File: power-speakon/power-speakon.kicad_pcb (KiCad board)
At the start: 4 copper layers, 65 x 24 mm, 18 parts, among them J101 NL4MDXX-V-3, J102 NL4MDXX-V-3, J103 WAGO 2601-1101, J104 WAGO 2601-1101, Q201 BSC010N04LS, Q202 BSC010N04LS, U201 LM74502-Q1

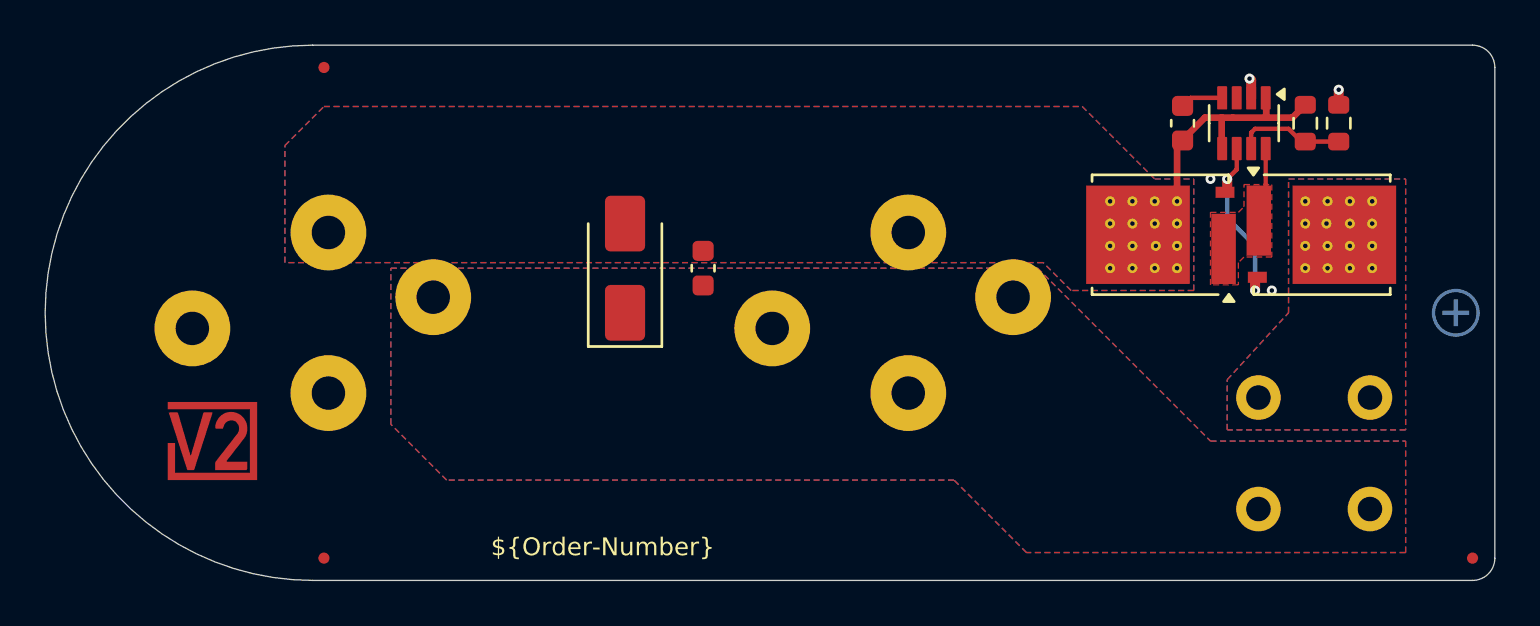
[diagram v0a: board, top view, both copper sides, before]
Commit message: Update power symbols
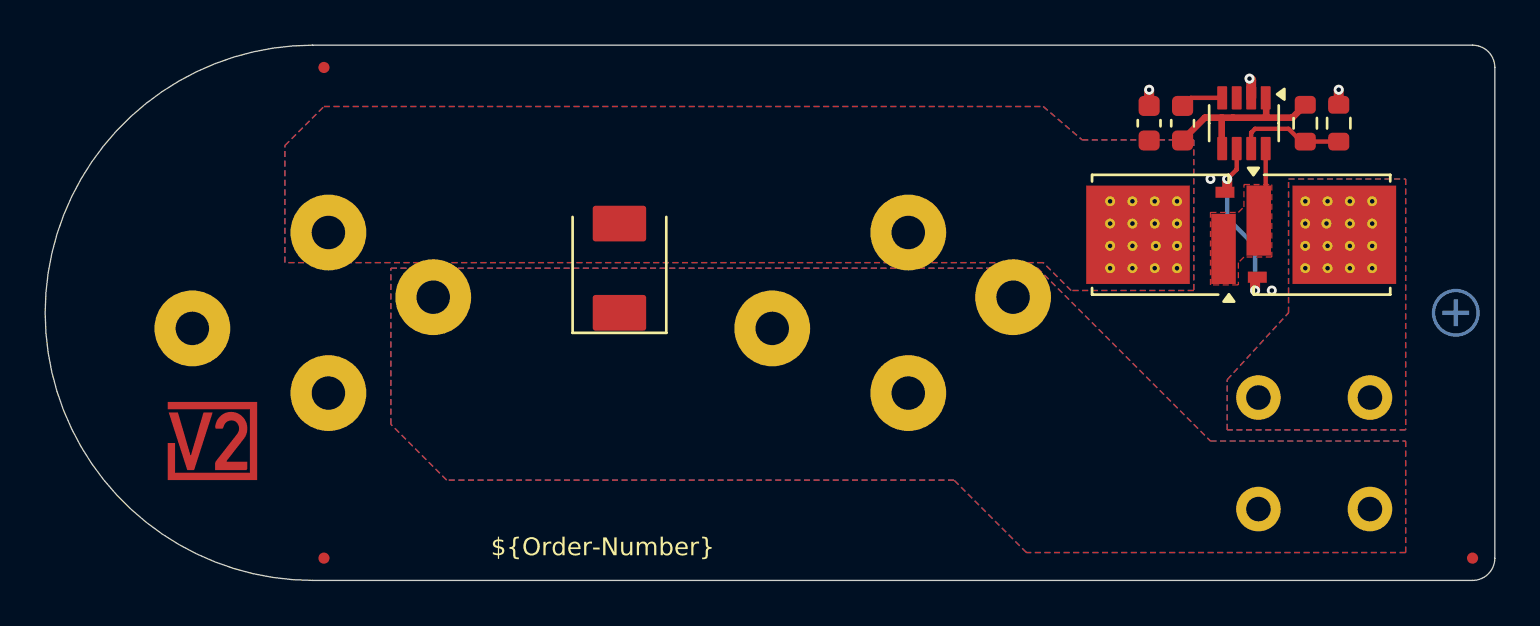
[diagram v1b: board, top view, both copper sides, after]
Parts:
- C201, C202: footprint Capacitor_SMD:C_0603_1608Metric -> V2_Capacitor_SMD:C_0603
- FID101, FID102, FID103: value Fiducial -> Fiducial_Paste
- INFO101: value ORDER-NUMBER -> Order_Number
- R201, R202: footprint Resistor_SMD:R_0603_1608Metric -> V2_Resistor_SMD:R_0603
- TVS101: value SMAJ36CA -> SMBJ36CA; footprint Diode_SMD:D_SMA -> V2_Diode_SMD:D_SMB
- moved C201 21.0 mm to (152.2, 83.2), turned to 90 degrees
- moved TVS101 0.25 mm to (128.5, 89.8)
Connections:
- net /+24V-Socket renamed /+24V-Supply
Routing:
- net /+24V-Supply: track 11.3 -> 8.83 mm
- net GND: track 1.57 -> 2.29 mm, vias 4 -> 5

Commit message: Fix WAGOs
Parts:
- moved J104 1.50 mm to (160.2, 98.8)
- moved ICON102 0.25 mm to (166.0, 91.5)
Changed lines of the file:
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@@
 	(footprint "V2_Artwork:Plus_Small"
 		(layer "B.Cu")
-		(at 166 91.75 180)
+		(at 166 91.5 180)
 		(property "Reference" "ICON102"
 			(at 0 2.5 0)
@@
 	(footprint "V2_Connector_WAGO:2601-1101"
 		(layer "B.Cu")
-		(at 160.25 100.25 -90)
+		(at 160.25 98.75 -90)
 		(property "Reference" "J104"
 			(at 0.1 12 90)
@@
 		)
 		(fp_text user "${REFERENCE}"
-			(at 0 0 180)
-			(layer "B.Fab")
-			(effects
+			(at 0 0 0)
+			(layer "B.Fab")
+			(effects

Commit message: Refresh
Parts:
- J101, J102: footprint V2_Connector_Audio:Jack_speakON_Neutrik_NL4MDXX-V-3_Vertical -> V2_Connector_SpeakOn:Jack_speakON_Neutrik_NL4MDXX-V-3_Vertical
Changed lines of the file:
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@@
 				(font
 					(size 0.5 0.5)
-					(thickness 0.05)
+					(thickness 0.1)
+					(bold yes)
 				)
 			)
@@
 		)
 		(fp_rect
-			(start -1.48 -0.73)
-			(end 1.48 0.73)
+			(start -1.23 -0.73)
+			(end 1.23 0.73)
 			(stroke
 				(width 0.05)
@@
 		)
 		(pad "1" smd roundrect
-			(at -0.775 0 90)
-			(size 0.9 0.95)
+			(at -0.7 0 90)
+			(size 0.7 0.8)
 			(layers "F.Cu" "F.Mask" "F.Paste")
-			(roundrect_rratio 0.25)
+			(roundrect_rratio 0.1428571429)
 			(net 12 "/+24V-Supply")
 			(pintype "passive")
 		)
 		(pad "2" smd roundrect
-			(at 0.775 0 90)
-			(size 0.9 0.95)
+			(at 0.7 0 90)
+			(size 0.7 0.8)
 			(layers "F.Cu" "F.Mask" "F.Paste")
-			(roundrect_rratio 0.25)
+			(roundrect_rratio 0.1428571429)
 			(net 1 "GND")
 			(pintype "passive")
@@
 		)
 		(fp_rect
-			(start -1.48 -0.73)
-			(end 1.48 0.73)
+			(start -1.23 -0.73)
+			(end 1.23 0.73)
 			(stroke
 				(width 0.05)
@@
 		)
 		(pad "1" smd roundrect
-			(at -0.825 0 90)
-			(size 0.8 0.95)
+			(at -0.75 0 90)
+			(size 0.75 0.95)
 			(layers "F.Cu" "F.Mask" "F.Paste")
-			(roundrect_rratio 0.25)
+			(roundrect_rratio 0.1333333333)
 			(net 10 "/Polarity Protection/Overvoltage")
 			(pintype "passive")
 		)
 		(pad "2" smd roundrect
-			(at 0.825 0 90)
-			(size 0.8 0.95)
+			(at 0.75 0 90)
+			(size 0.75 0.95)
 			(layers "F.Cu" "F.Mask" "F.Paste")
-			(roundrect_rratio 0.25)
+			(roundrect_rratio 0.1333333333)
 			(net 1 "GND")
 			(pintype "passive")
@@
 			(effects
 				(font
-					(size 0.75 0.75)
+					(size 0.5 0.5)
 					(thickness 0.1)
 				)
@@
 				(font
 					(size 0.5 0.5)
-					(thickness 0.05)
+					(thickness 0.1)
+					(bold yes)
 				)
 			)
@@
 			(effects
 				(font
-					(size 0.75 0.75)
+					(size 0.5 0.5)
 					(thickness 0.1)
 				)
@@
 		)
 		(fp_rect
-			(start -1.48 -0.73)
-			(end 1.48 0.73)
+			(start -1.23 -0.73)
+			(end 1.23 0.73)
 			(stroke
 				(width 0.05)
@@
 		)
 		(pad "1" smd roundrect
-			(at -0.775 0 90)
-			(size 0.9 0.95)
+			(at -0.7 0 90)
+			(size 0.7 0.8)
 			(layers "F.Cu" "F.Mask" "F.Paste")
-			(roundrect_rratio 0.25)
+			(roundrect_rratio 0.1428571429)
 			(net 12 "/+24V-Supply")
 			(pintype "passive")
 		)
 		(pad "2" smd roundrect
-			(at 0.775 0 90)
-			(size 0.9 0.95)
+			(at 0.7 0 90)
+			(size 0.7 0.8)
 			(layers "F.Cu" "F.Mask" "F.Paste")
-			(roundrect_rratio 0.25)
+			(roundrect_rratio 0.1428571429)
 			(net 7 "Net-(U201-VCAP)")
 			(pintype "passive")
@@
 		)
 		(fp_rect
-			(start -1.48 -0.73)
-			(end 1.48 0.73)
+			(start -1.23 -0.73)
+			(end 1.23 0.73)
 			(stroke
 				(width 0.05)
@@
 		)
 		(pad "1" smd roundrect
-			(at -0.825 0 270)
-			(size 0.8 0.95)
+			(at -0.75 0 270)
+			(size 0.75 0.95)
 			(layers "F.Cu" "F.Mask" "F.Paste")
-			(roundrect_rratio 0.25)
+			(roundrect_rratio 0.1333333333)
 			(net 12 "/+24V-Supply")
 			(pintype "passive")
 		)
 		(pad "2" smd roundrect
-			(at 0.825 0 270)
-			(size 0.8 0.95)
+			(at 0.75 0 270)
+			(size 0.75 0.95)
 			(layers "F.Cu" "F.Mask" "F.Paste")
-			(roundrect_rratio 0.25)
+			(roundrect_rratio 0.1333333333)
 			(net 10 "/Polarity Protection/Overvoltage")
 			(pintype "passive")
@@
 			(effects
 				(font
-					(size 0.75 0.75)
+					(size 0.5 0.5)
 					(thickness 0.1)
 					(bold yes)
@@
 		)
 		(embedded_fonts no)
-		(model "/Users/kay/Documents/KiCad/9.0/versioduo.kicad/3dmodels/V2_Connector_WAGO.3dshapes/2601-1101.stp"
+		(model "../../3dmodels/V2_Connector_WAGO.3dshapes/2601-1101.stp"
 			(offset
 				(xyz 1.36 -1.9 0)
@@
 		(embedded_fonts no)
 	)
-	(footprint "V2_Connector_Audio:Jack_speakON_Neutrik_NL4MDXX-V-3_Vertical"
+	(footprint "V2_Connector_SpeakOn:Jack_speakON_Neutrik_NL4MDXX-V-3_Vertical"
 		(layer "B.Cu")
 		(at 140.75 91.75 180)
@@
 			(layer "B.Fab")
 		)
+		(fp_text user "${REFERENCE}"
+			(at 0 0 0)
+			(layer "B.Fab")
+			(effects
+				(font
+					(size 0.75 0.75)
+					(thickness 0.1)
+				)
+				(justify mirror)
+			)
+		)
 		(pad "1+" thru_hole circle
 			(at -0.7 3.6 180)
@@
 		)
 	)
-	(footprint "V2_Connector_Audio:Jack_speakON_Neutrik_NL4MDXX-V-3_Vertical"
+	(footprint "V2_Connector_SpeakOn:Jack_speakON_Neutrik_NL4MDXX-V-3_Vertical"
 		(layer "B.Cu")
 		(at 114.75 91.75 180)
@@
 			(layer "B.Fab")
 		)
+		(fp_text user "${REFERENCE}"
+			(at 0 0 0)
+			(layer "B.Fab")
+			(effects
+				(font
+					(size 0.75 0.75)
+					(thickness 0.1)
+				)
+				(justify mirror)
+			)
+		)
 		(pad "1+" thru_hole circle
 			(at -0.7 3.6 180)
@@
 		)
 		(fp_text user "${REFERENCE}"
-			(at 0 0 0)
+			(at 0 0 180)
 			(layer "B.Fab")
 			(effects
 				(font
-					(size 0.75 0.75)
+					(size 0.5 0.5)
 					(thickness 0.1)
 					(bold yes)
@@
 		)
 		(embedded_fonts no)
-		(model "/Users/kay/Documents/KiCad/9.0/versioduo.kicad/3dmodels/V2_Connector_WAGO.3dshapes/2601-1101.stp"
+		(model "../../3dmodels/V2_Connector_WAGO.3dshapes/2601-1101.stp"
 			(offset
 				(xyz 1.36 -1.9 0)
@@
 		)
 	)
-	(gr_arc
-		(start 114.75 103.75)
-		(mid 102.75 91.75)
-		(end 114.75 79.75)
-		(stroke
-			(width 0.05)
-			(type solid)
-		)
-		(layer "Edge.Cuts")
-	)
 	(gr_line
 		(start 114.75 79.75)
@@
 		(layer "Edge.Cuts")
 	)
-	(gr_line
-		(start 167.75 80.75)
-		(end 167.75 102.75)
+	(gr_arc
+		(start 114.75 103.75)
+		(mid 102.75 91.75)
+		(end 114.75 79.75)
 		(stroke
 			(width 0.05)
@@
 		(layer "Edge.Cuts")
 	)
-	(gr_arc
-		(start 167.75 102.75)
-		(mid 167.457107 103.457107)
+	(gr_line
+		(start 114.75 103.75)
 		(end 166.75 103.75)
 		(stroke
@@
 	)
 	(gr_line
-		(start 114.75 103.75)
+		(start 167.75 80.75)
+		(end 167.75 102.75)
+		(stroke
+			(width 0.05)
+			(type solid)
+		)
+		(layer "Edge.Cuts")
+	)
+	(gr_arc
+		(start 167.75 102.75)
+		(mid 167.457107 103.457107)
 		(end 166.75 103.75)
 		(stroke

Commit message: Update library
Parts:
- J101, J102: footprint V2_Connector_SpeakOn:Jack_speakON_Neutrik_NL4MDXX-V-3_Vertical -> V2_Connector_SpeakOn:NL4MDXX-V-3
- TVS101: value SMBJ36CA -> SMBJ33CA
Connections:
- net +24V renamed +28V
- net /+24V-Supply renamed /+28V-Supply

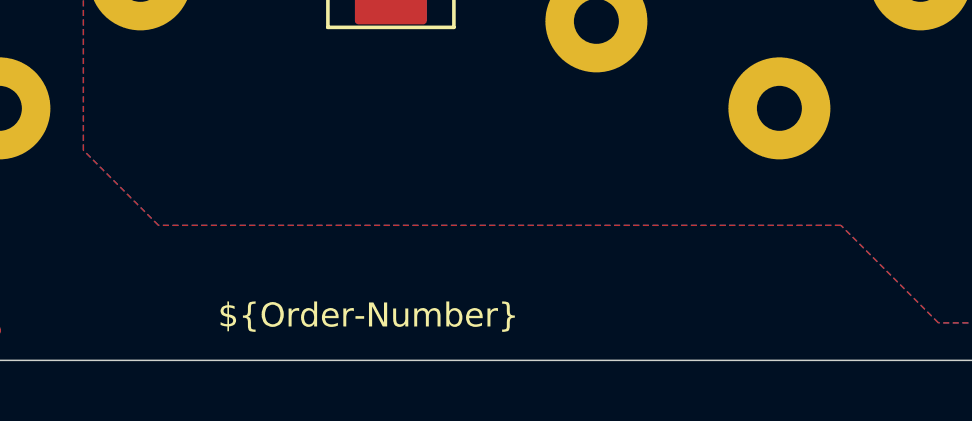
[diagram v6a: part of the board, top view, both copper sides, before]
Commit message: Replace Order_Number
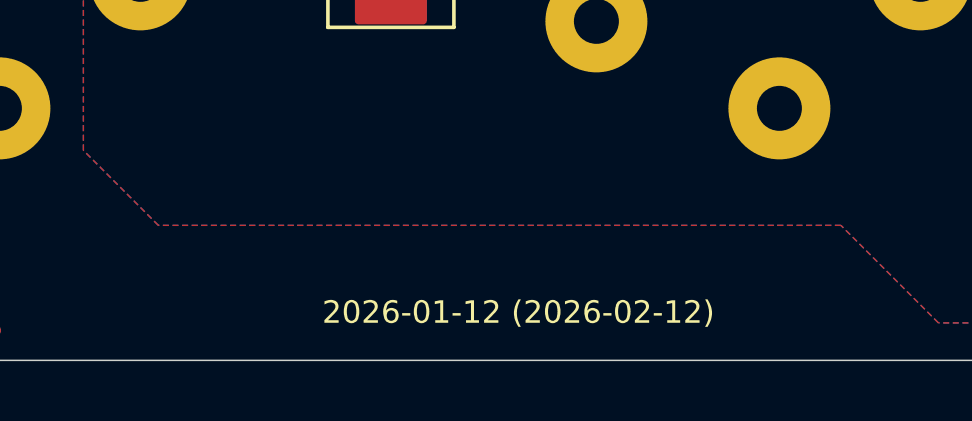
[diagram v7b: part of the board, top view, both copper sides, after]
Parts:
- INFO101: value Order_Number -> ~; footprint V2_Production:Order_Number -> V2_Production:Revision
- moved INFO101 5.00 mm to (132.8, 102.2)
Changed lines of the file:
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@@
 	(paper "A4")
 	(title_block
-		(date "2026-02-10")
+		(date "2026-02-12")
 		(rev "2026-01-12")
 	)
@@
 		)
 	)
-	(property "Order-Number" "JLCJLCJLCJLC")
 	(net 0 "")
 	(net 1 "GND")
@@
 			)
 		)
-		(property "Description" ""
+		(property "Description" "Transient Voltage Suppressor Diode, Bidirectional, 36.7-40.6V"
 			(at 0 0 90)
 			(unlocked yes)
@@
 			)
 		)
-		(property "Description" ""
+		(property "Description" "Unpolarized capacitor, small symbol"
 			(at 0 0 90)
 			(layer "F.Fab")
@@
 			)
 		)
-		(property "Description" ""
+		(property "Description" "Fiducial Marker"
 			(at 0 0 0)
 			(unlocked yes)
@@
 			)
 		)
-		(property "Description" ""
+		(property "Description" "Resistor, small symbol"
 			(at 0 0 90)
 			(layer "F.Fab")
@@
 		)
 	)
-	(footprint "V2_Production:Order_Number"
+	(footprint "V2_Production:Revision"
 		(layer "F.Cu")
-		(at 127.75 102.25)
+		(at 132.75 102.15)
 		(property "Reference" "INFO101"
 			(at 0 -1.77 0)
@@
 			)
 		)
-		(property "Value" "Order_Number"
+		(property "Value" "~"
 			(at 0 2.27 0)
 			(unlocked yes)
@@
 		(sheetname "/")
 		(sheetfile "power-speakon.kicad_sch")
-		(attr exclude_from_pos_files exclude_from_bom)
-		(fp_rect
-			(start -7 -0.75)
-			(end 7 0.75)
-			(stroke
-				(width 0.05)
-				(type default)
+		(attr exclude_from_pos_files exclude_from_bom allow_missing_courtyard)
+		(fp_text user "${REVISION} (${ISSUE_DATE})"
+			(at 0 0 0)
+			(unlocked yes)
+			(layer "F.SilkS")
+			(effects
+				(font
+					(size 0.75 0.75)
+					(thickness 0.1)
+				)
 			)
-			(fill no)
-			(layer "F.CrtYd")
 		)
-		(fp_text user "${Order-Number}"
+		(fp_text user "${REVISION} (${ISSUE_DATE})"
 			(at 0 0 0)
 			(unlocked yes)
-			(layer "F.SilkS")
+			(layer "F.Fab")
 			(effects
 				(font
-					(size 0.8 0.8)
-					(thickness 0.12)
+					(size 0.75 0.75)
+					(thickness 0.1)
 				)
 			)
@@
 			)
 		)
-		(property "Description" ""
+		(property "Description" "Fiducial Marker"
 			(at 0 0 0)
 			(unlocked yes)
@@
 			)
 		)
-		(property "Description" ""
+		(property "Description" "Reverse Polarity Protection Controller"
 			(at 0 0 270)
 			(unlocked yes)
@@
 			)
 		)
-		(property "Description" ""
+		(property "Description" "Unpolarized capacitor, small symbol"
 			(at 0 0 90)
 			(layer "F.Fab")
@@
 			)
 		)
-		(property "Description" ""
+		(property "Description" "Resistor, small symbol"
 			(at 0 0 270)
 			(layer "F.Fab")
@@
 			)
 		)
-		(property "Description" ""
+		(property "Description" "Fiducial Marker"
 			(at 0 0 0)
 			(unlocked yes)
@@
 			)
 		)
-		(property "Sim.Enable" "0"
-			(at 0 0 0)
-			(unlocked yes)
-			(layer "F.Fab")
-			(hide yes)
-			(effects
-				(font
-					(size 1 1)
-					(thickness 0.15)
-				)
-			)
-		)
 		(sheetname "/")
 		(sheetfile "power-speakon.kicad_sch")
@@
 			)
 		)
-		(property "Sim.Enable" "0"
-			(at 0 0 180)
-			(unlocked yes)
-			(layer "B.Fab")
-			(hide yes)
-			(effects
-				(font
-					(size 1 1)
-					(thickness 0.15)
-				)
-				(justify mirror)
-			)
-		)
 		(sheetname "/")
 		(sheetfile "power-speakon.kicad_sch")
@@
 			)
 		)
-		(property "Datasheet" ""
+		(property "Datasheet" "https://www.neutrik.com/en/product/nl4mdxx-v-3"
 			(at -0.7 3.6 0)
 			(unlocked yes)
@@
 			)
 		)
-		(property "Description" ""
+		(property "Description" "speakON Chassis Connectors, 4 pole chassis connector, grey D-size flange, self tapping screw holes (A-screw), vertical PCB mount. Replaces NL4MD-V-1"
 			(at -0.7 3.6 0)
 			(unlocked yes)
@@
 			(remove_unused_layers yes)
 			(keep_end_layers yes)
-			(zone_layer_connections "In1.Cu" "In2.Cu")
+			(zone_layer_connections)
 			(net 1 "GND")
 			(pinfunction "1-")
@@
 			)
 		)
-		(property "Datasheet" ""
+		(property "Datasheet" "https://www.neutrik.com/en/product/nl4mdxx-v-3"
 			(at -0.7 3.6 0)
 			(unlocked yes)
@@
 			)
 		)
-		(property "Description" ""
+		(property "Description" "speakON Chassis Connectors, 4 pole chassis connector, grey D-size flange, self tapping screw holes (A-screw), vertical PCB mount. Replaces NL4MD-V-1"
 			(at -0.7 3.6 0)
 			(unlocked yes)
@@
 			(remove_unused_layers yes)
 			(keep_end_layers yes)
-			(zone_layer_connections "In1.Cu" "In2.Cu")
+			(zone_layer_connections)
 			(net 1 "GND")
 			(pinfunction "1-")
@@
 			(remove_unused_layers yes)
 			(keep_end_layers yes)
-			(zone_layer_connections "In1.Cu" "In2.Cu")
+			(zone_layer_connections)
 			(net 1 "GND")
 			(pintype "passive")
@@
 			(remove_unused_layers yes)
 			(keep_end_layers yes)
-			(zone_layer_connections "In1.Cu" "In2.Cu")
+			(zone_layer_connections)
 			(net 1 "GND")
 			(pintype "passive")
